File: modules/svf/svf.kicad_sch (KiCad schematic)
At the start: 22 parts, among them U1 MCP6002-xSN, U2 MCP6002-xSN

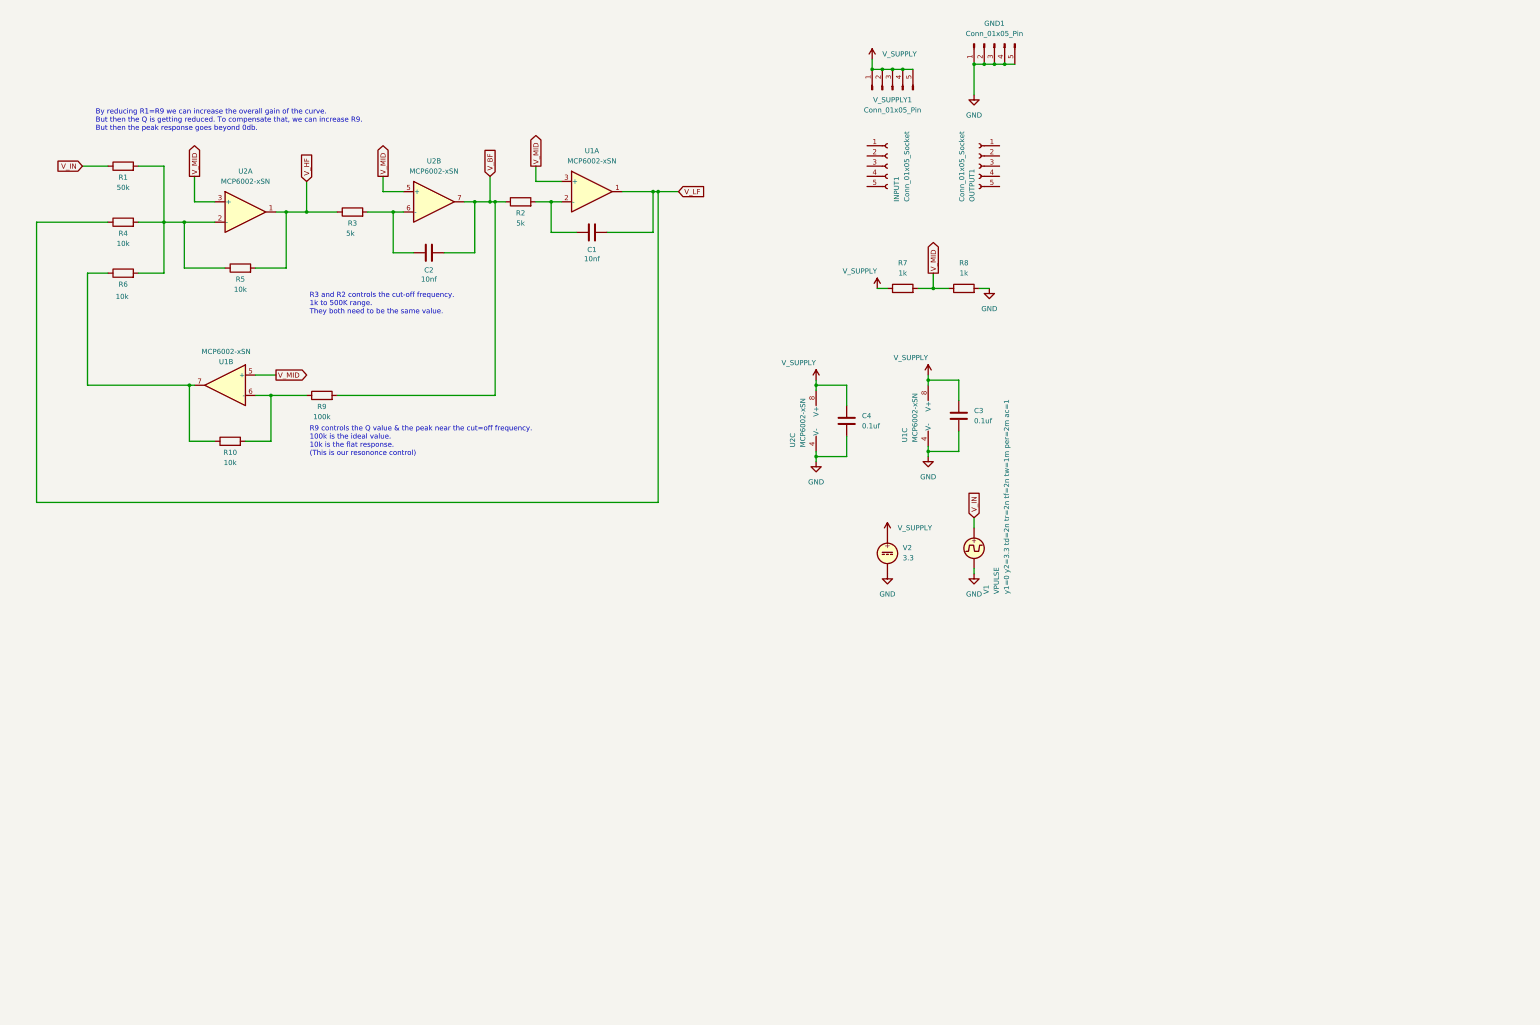
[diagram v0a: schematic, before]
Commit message: Implement the base filter simulation
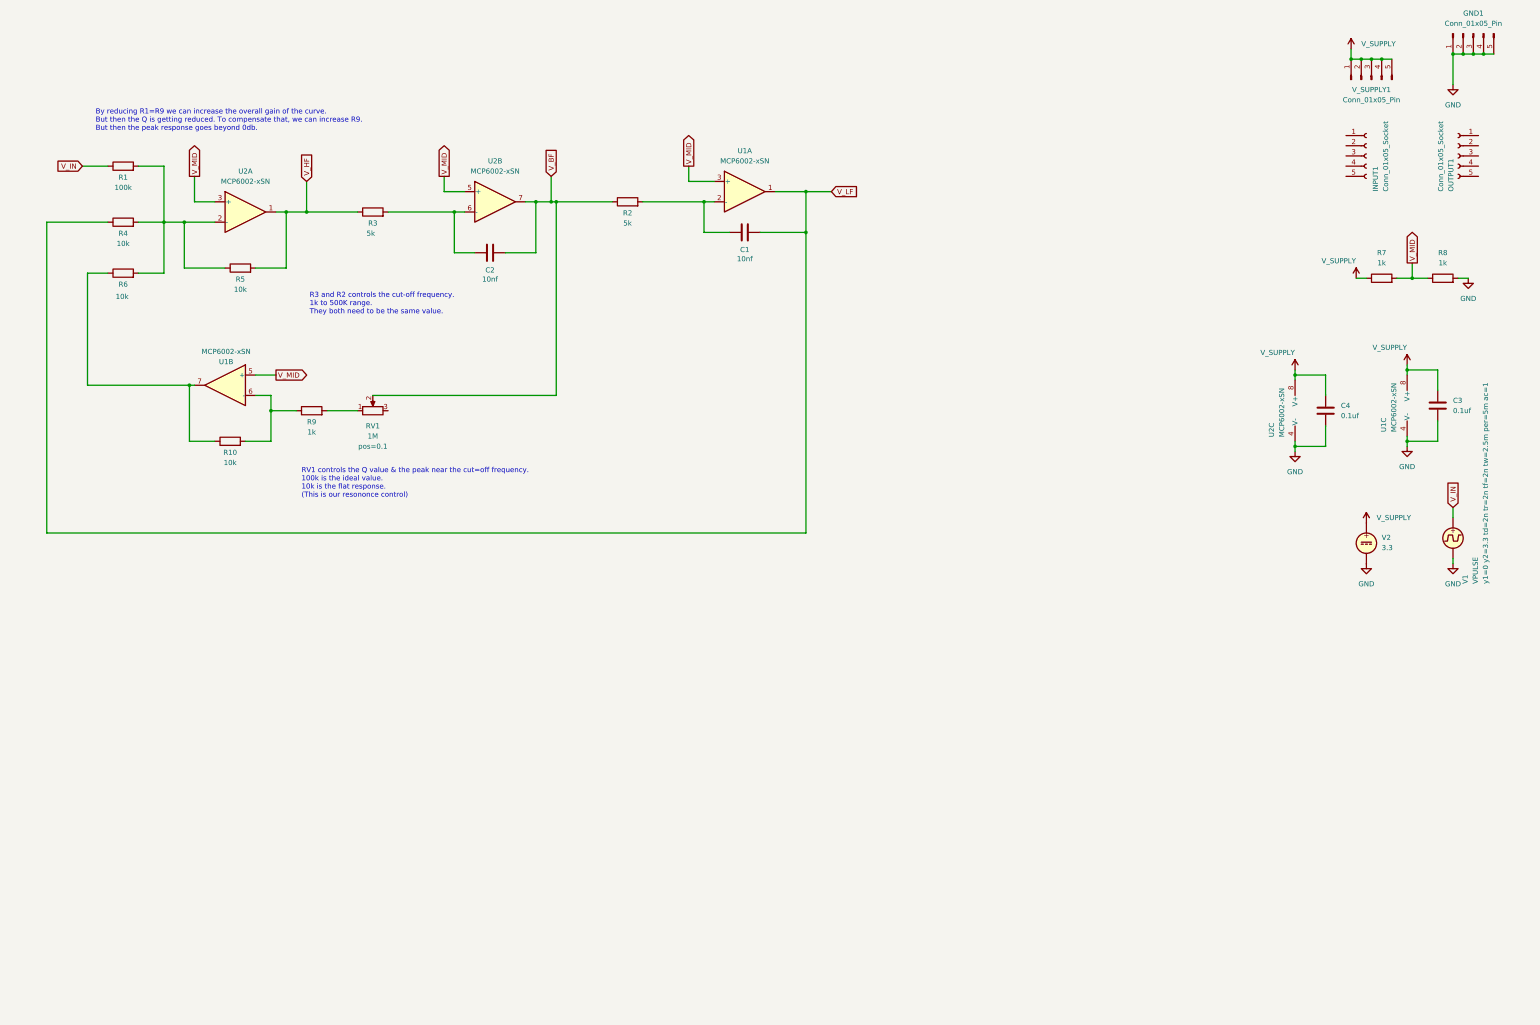
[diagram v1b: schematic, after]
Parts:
- added RV1: 1M, symbol Device:R_Potentiometer
- R1: value 50k -> 100k
- R9: value 100k -> 1k
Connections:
- net V_BF: now also RV1.2; no longer R9.2
- new net: R9.2, RV1.1
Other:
- note added: "RV1 controls the Q value & the peak near the cut=off frequency. 100k is the ideal value. 10k is the flat response. (This is our resononce control)"
- note removed: "R9 controls the Q value & the peak near the cut=off frequency. 100k is the ideal value. 10k is the flat response. (This is our resononce control)"
- moved on the sheet: C1, C2, C3, C4, GND1, INPUT1, OUTPUT1, R2, R3, R7, R8, U1A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

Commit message: Implement the final schematic for SVF
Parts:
- removed R2, R3: 5k, symbol Device:R
- added C5: 0.1uf, symbol Device:C
- added R11, R12, R13, R16: 1k, symbol Device:R
- added R14, R15: 1M, symbol Device:R
- added R17: 100k, symbol Device:R
- added RV2, RV3: 50k, symbol Device:R_Potentiometer
- added U3: MCP6002-xSN, symbol Amplifier_Operational:MCP6002-xSN
- added U4, U5: VTL5C, BreadModular_MISC:VTL5C, symbol Isolator:VTL5C
- added V4: VSIN, symbol Simulation_SPICE:VSIN
- RV1: Comments (none) -> Q CONTROL
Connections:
- net GND: now also C5.2, R15.1, R16.1, RV3.1, U3.4 (V-), V4.2
- net V_BF: now also R12.2; no longer C2.2, RV1.2, U2.7
- net V_HF: now also R13.2; no longer R5.2, U2.1
- net V_LF: now also R11.2; no longer C1.2, R4.1, U1.1
- net V_SUPPLY: now also C5.1, RV3.3, U3.8 (V+)
- net at C1.1, U1.2 (-): now also U5.3
- net at C2.1, U2.6 (-): now also U4.3
- new net: R13.1, R5.2, U2.1, U4.4
- new net: C1.2, R11.1, R4.1, U1.1
- new net: C2.2, R12.1, RV1.2, U2.7, U5.4
- new net: R16.2, RV2.3
- new net: R17.1, RV3.2
- new net: R14.1, R15.2, U3.3 (+)
- new net VACTROL_NEG: RV2.2, U3.2 (-), U4.1 (-), U5.1 (-)
- new net VACTROL_POS: U3.1, U4.2 (+), U5.2 (+)
- new net V_CV: R14.2, R17.2, V4.1
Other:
- moved on the sheet: C3, C4, U1C, U2C, V1, V2

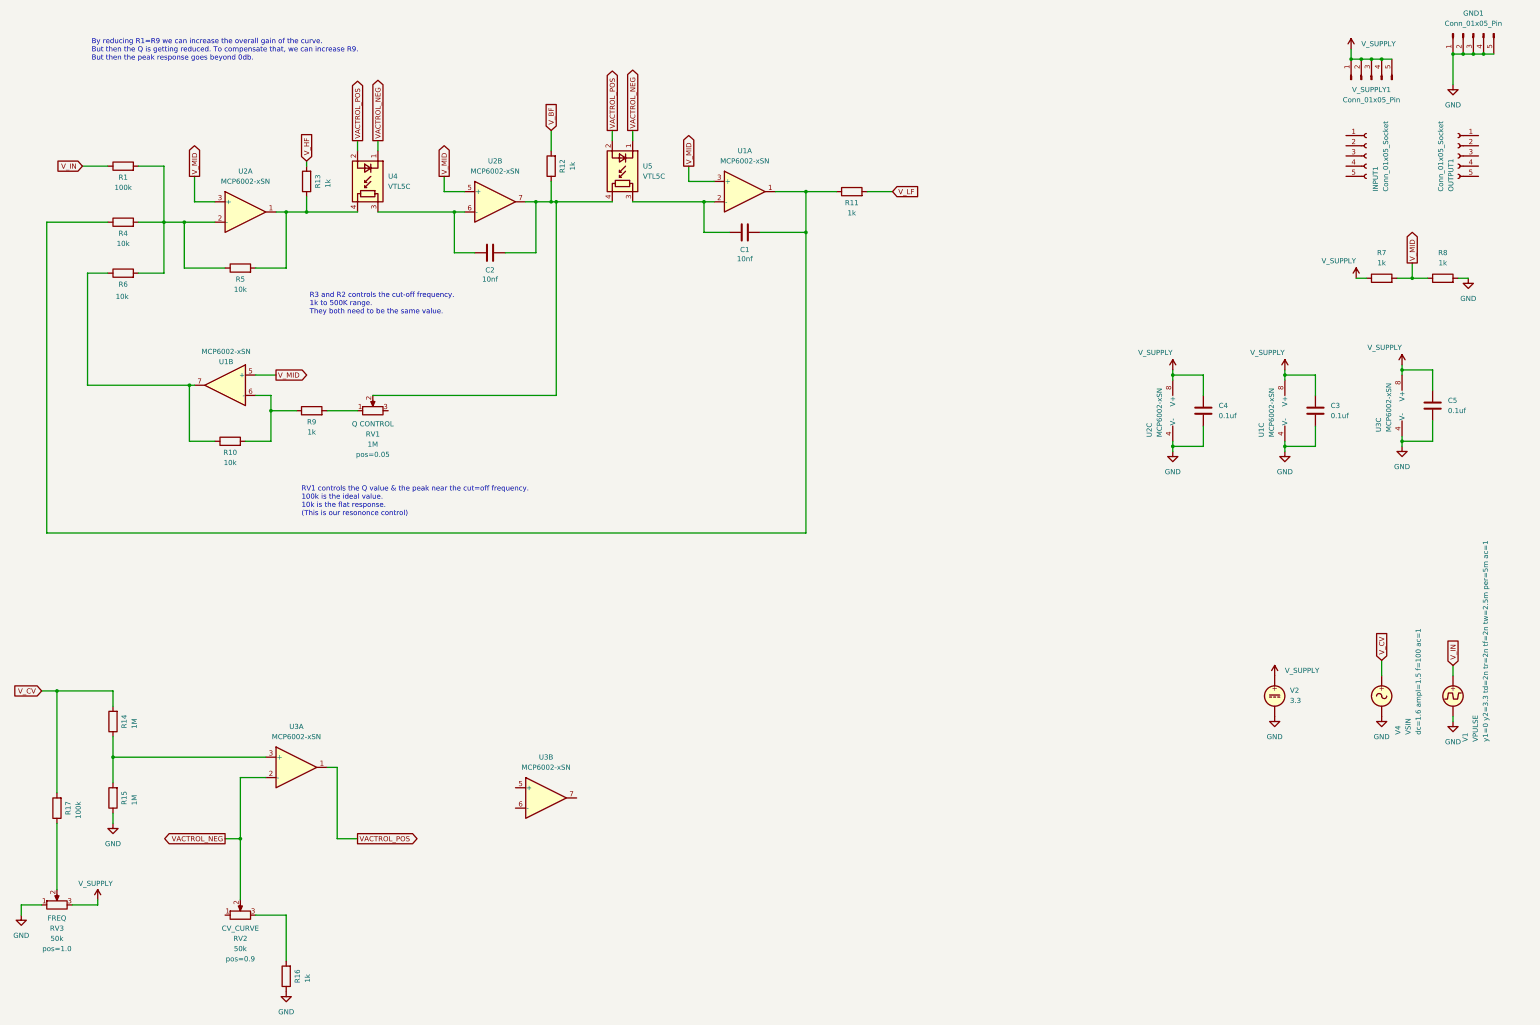
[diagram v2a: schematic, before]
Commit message: Add inline documentation for the SVF
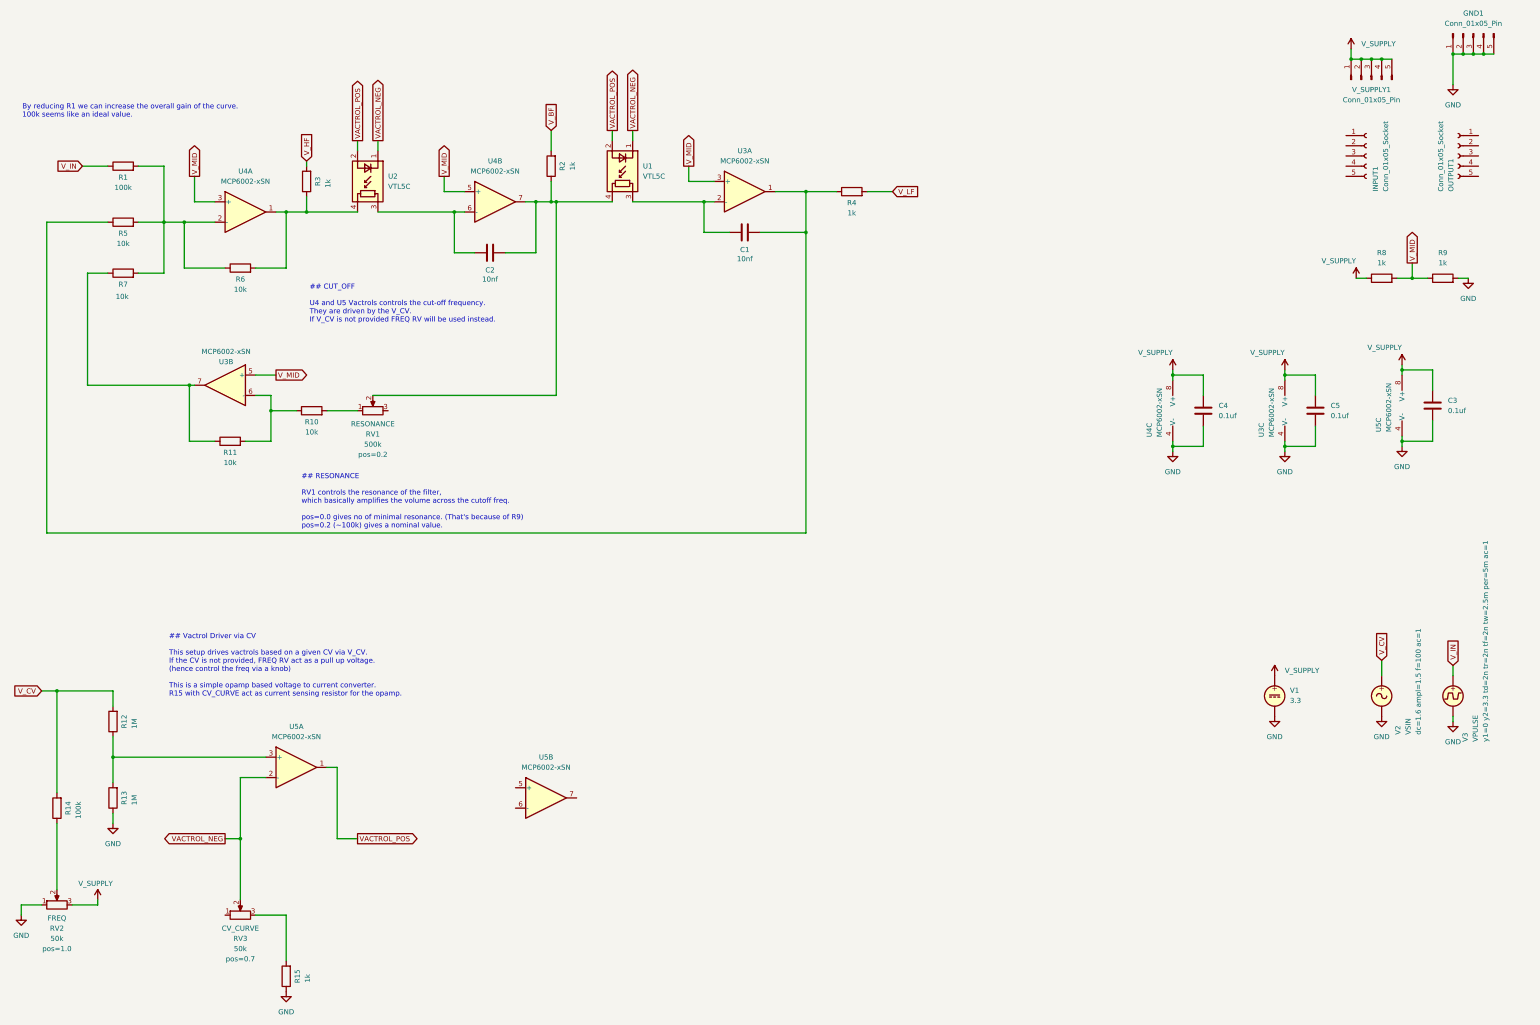
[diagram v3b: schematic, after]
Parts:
- R10: renamed from R9; value 1k -> 10k
- RV1: value 1M -> 500k; Comments Q CONTROL -> RESONANCE
- renumbered C5 to C3, C3 to C5, R10 to R11, R14 to R12, R15 to R13, R17 to R14, R16 to R15, R12 to R2, R13 to R3, R11 to R4, R4 to R5, R5 to R6, R6 to R7, R7 to R8, R8 to R9, RV3 to RV2, RV2 to RV3, U5 to U1, U4 to U2, U1 to U3, U2 to U4, U3 to U5, V2 to V1, V4 to V2, V1 to V3
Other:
- note added: "## CUT_OFF U4 and U5 Vactrols controls the cut-off frequency. They are driven by the V_CV. If V_CV is not provided FREQ RV will be used instead."
- note added: "## RESONANCE RV1 controls the resonance of the filter, which basically amplifies the volume across the cutoff freq. pos=0.0 gives no of minimal resonance. (That's because of R9) pos=0.2 (~100k) gives a nominal value."
- note added: "## Vactrol Driver via CV This setup drives vactrols based on a given CV via V_CV. If the CV is not provided, FREQ RV act as a pull up voltage. (hence control the freq via a knob) This is a simple opamp based voltage to current converter. R15 with CV_CURVE act as current sensing resistor for the opamp."
- note added: "By reducing R1 we can increase the overall gain of the curve. 100k seems like an ideal value."
- note removed: "By reducing R1=R9 we can increase the overall gain of the curve. But then the Q is getting reduced. To compensate that, we can increase R9. But then the peak response goes beyond 0db."
- note removed: "R3 and R2 controls the cut-off frequency. 1k to 500K range. They both need to be the same value."
- note removed: "RV1 controls the Q value & the peak near the cut=off frequency. 100k is the ideal value. 10k is the flat response. (This is our resononce control)"

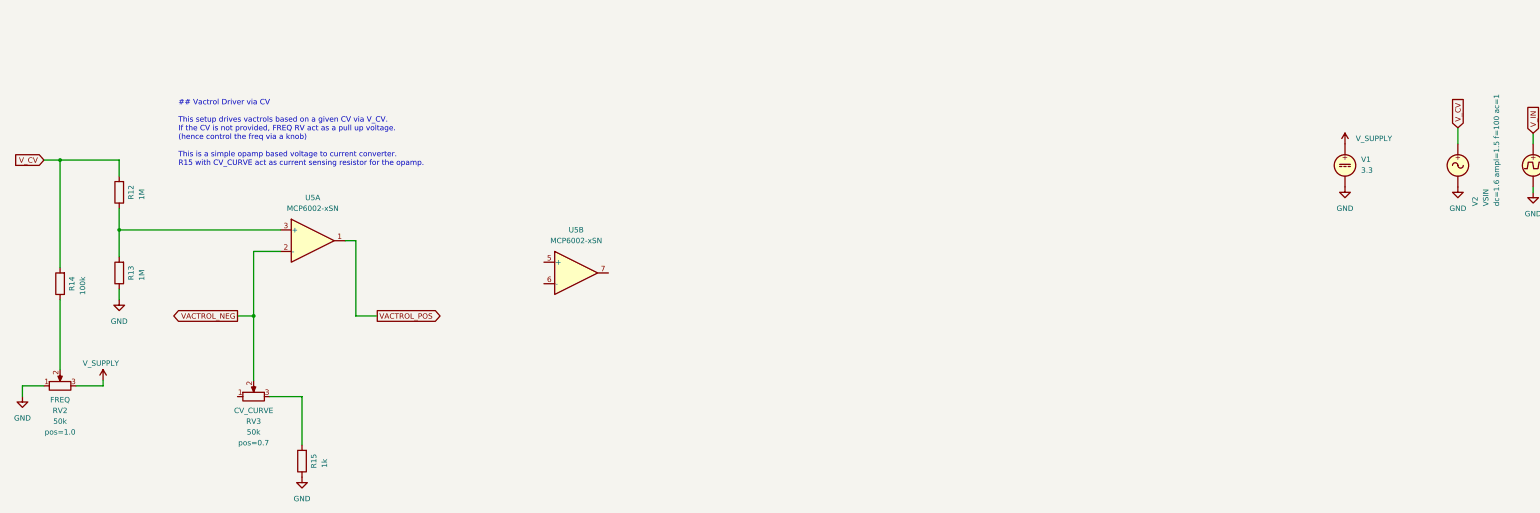
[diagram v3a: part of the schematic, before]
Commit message: Simplify the SVF design with just freq & resonance knobs
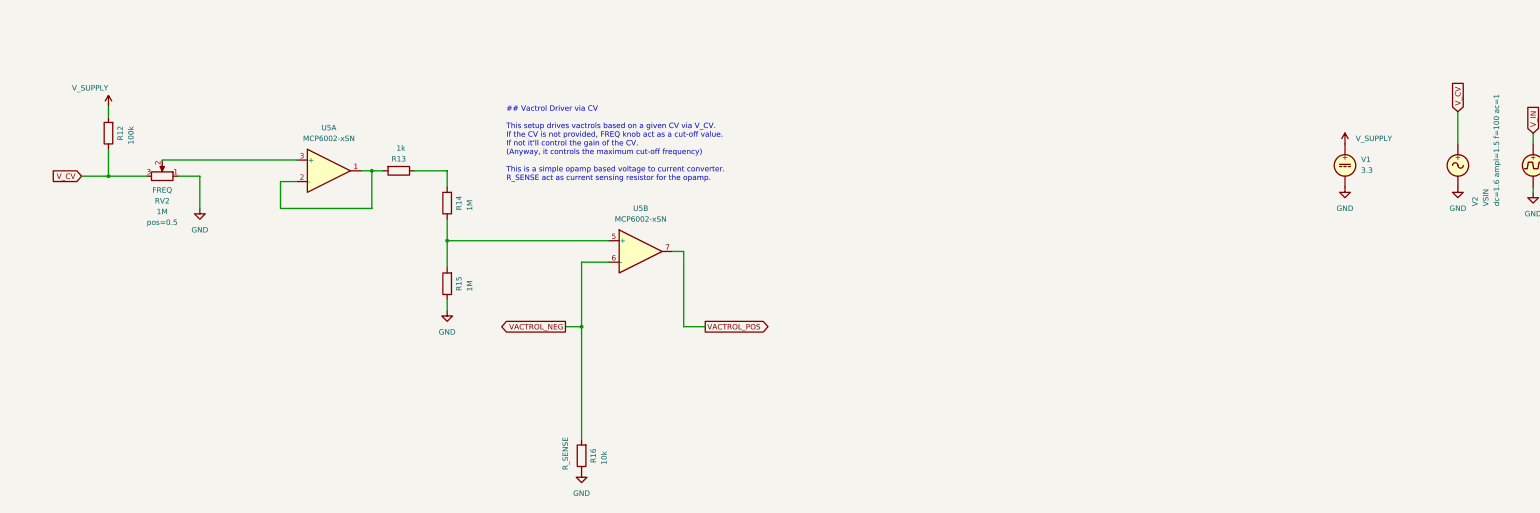
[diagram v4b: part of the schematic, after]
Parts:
- removed R14: 100k, symbol Device:R
- removed RV3: 50k, symbol Device:R_Potentiometer
- added R12: 100k, symbol Device:R
- added R13: 1k, symbol Device:R
- R16: renamed from R15; value 1k -> 10k
- RV2: value 50k -> 1M
- renumbered R12 to R14, R13 to R15
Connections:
- net VACTROL_NEG: now also R16.2, U5.6 (-); no longer U5.2 (-)
- net VACTROL_POS: now also U5.7; no longer U5.1
- net V_CV: now also RV2.3, R12.1; no longer R14.2
- net V_SUPPLY: now also R12.2; no longer RV2.3
- net at RV2.2: now also U5.3 (+)
- net at U5.5 (+): now also R14.1, R15.2
- new net: R13.2, U5.1, U5.2 (-)
- new net: R13.1, R14.2
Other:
- note added: "## Vactrol Driver via CV This setup drives vactrols based on a given CV via V_CV. If the CV is not provided, FREQ knob act as a cut-off value. If not it'll control the gain of the CV. (Anyway, it controls the maximum cut-off frequency) This is a simple opamp based voltage to current converter. R_SENSE act as current sensing resistor for the opamp."
- note removed: "## Vactrol Driver via CV This setup drives vactrols based on a given CV via V_CV. If the CV is not provided, FREQ RV act as a pull up voltage. (hence control the freq via a knob) This is a simple opamp based voltage to current converter. R15 with CV_CURVE act as current sensing resistor for the opamp."
- moved on the sheet: R14, R15, R16

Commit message: Getting it ready for PCB routing
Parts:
- C1, C2, C3, C4, C5: footprint (none) -> Capacitor_SMD:C_0402_1005Metric
- R1, R10, R11, R12, R13, R14, R15, R16, R2, R3, R4, R5, R6, R7, R8, R9: footprint (none) -> Resistor_SMD:R_0402_1005Metric
- RV1, RV2: footprint (none) -> BreadModular_Pots:Potentiometer_RV09
- U3, U4, U5: footprint (none) -> Package_SO:SOIC-8-1EP_3.9x4.9mm_P1.27mm_EP2.29x3mm
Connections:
- net V_BF: now also OUTPUT1.5 (Pin_5)
- net V_CV: now also INPUT1.2 (Pin_2)
- net V_HF: now also OUTPUT1.3 (Pin_3), OUTPUT1.4 (Pin_4)
- net V_IN: now also INPUT1.1 (Pin_1)
- net V_LF: now also OUTPUT1.1 (Pin_1), OUTPUT1.2 (Pin_2)
- net at INPUT1.3 (Pin_3): now also INPUT1.4 (Pin_4), INPUT1.5 (Pin_5)
